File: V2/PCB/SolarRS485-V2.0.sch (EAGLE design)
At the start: 55 parts, among them J1 RJ45, J25 Grove-Serial, J33 Grove-Analog, J34 Grove-IO, J4 Grove-I2C, J6 7-segment LED, J8 RJ45, U1 MAX3485CSA, U2 +12v

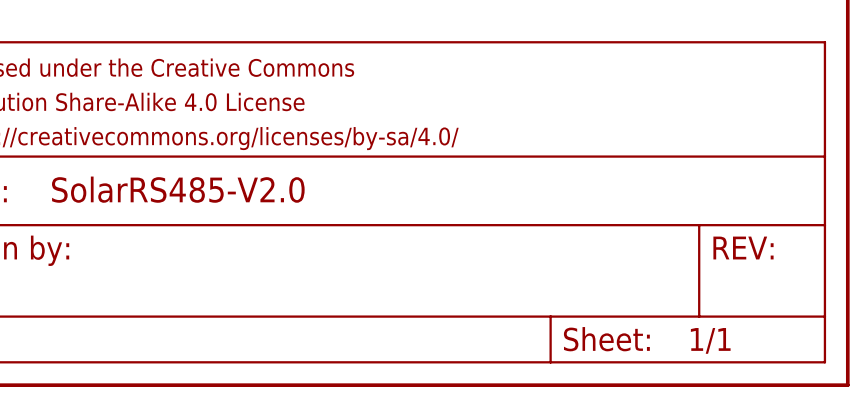
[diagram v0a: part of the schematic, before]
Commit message: Updated version number
Added some documentation / datasheets.

Added gitignore
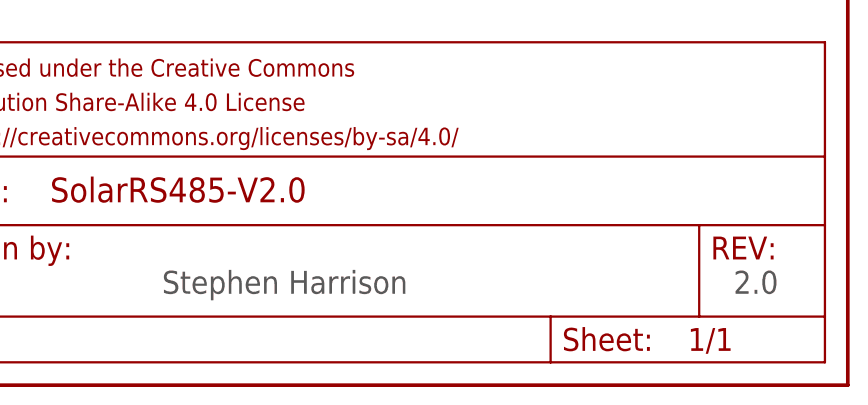
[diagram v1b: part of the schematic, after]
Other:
- note added: "2.0"
- note added: "Stephen Harrison"
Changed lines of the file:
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@@
 <wire x1="48.26" y1="53.34" x2="48.26" y2="2.54" width="0.1524" layer="97"/>
 <wire x1="223.52" y1="149.86" x2="223.52" y2="53.34" width="0.1524" layer="97"/>
+<text x="419.1" y="10.16" size="2.54" layer="97">2.0</text>
+<text x="355.6" y="10.16" size="2.54" layer="97">Stephen Harrison</text>
 </plain>
 <instances>
